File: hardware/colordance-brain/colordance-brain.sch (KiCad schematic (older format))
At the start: 21 parts, among them J1 Anderson, J5 RJ45, J6 RJ45, U1 AM26LS31x, U1 AP3211

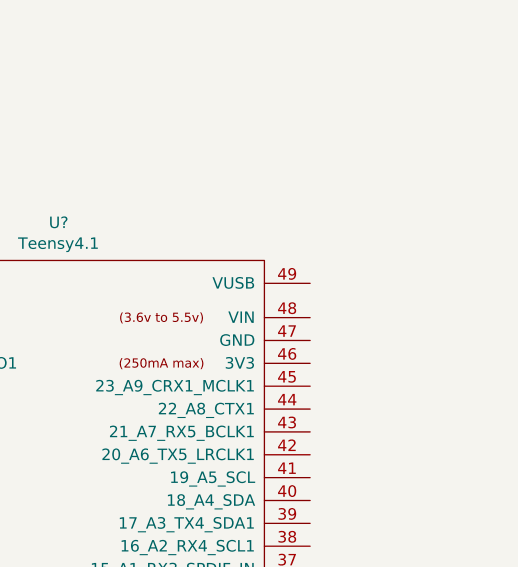
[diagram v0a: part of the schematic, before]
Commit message: Update pole node to v1.1
This adds lots of TVS diode, more decoupling, bulk caps on 5v and 12v
lines. Also adds pass-through Anderson connector.
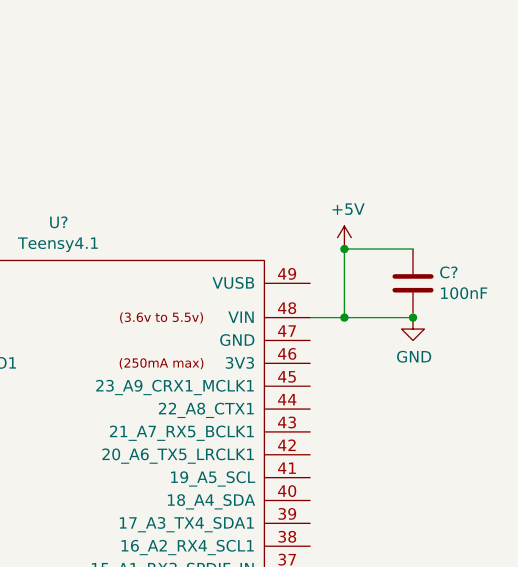
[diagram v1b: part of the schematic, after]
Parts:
- added C?: 100nF, symbol Device:C
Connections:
- net GND is gone; now on net +5V: C1.2, C1.2, C3.2, C?.2, C?.2, C?.2, C?.2, D1.2 (A), J1.2, J5.3, J5.4, J6.3, J6.4, R2.2, R5.2, U1.2 (GND), U1.8 (GND)
- net +5V: now also U?.48 (VIN), C?.1, C?.2
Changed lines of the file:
@@
 Wire Wire Line
 	1500 1250 1700 1250
+$Comp
+L power:+5V #PWR?
+U 1 1 60724EEF
+P 13100 2000
+F 0 "#PWR?" H 13100 1850 50  0001 C CNN
+F 1 "+5V" H 13115 2173 50  0000 C CNN
+F 2 "" H 13100 2000 50  0001 C CNN
+F 3 "" H 13100 2000 50  0001 C CNN
+	1    13100 2000
+	1    0    0    -1
+$EndComp
+Wire Wire Line
+	12950 2300 13100 2300
+Wire Wire Line
+	13100 2300 13100 2000
+$Comp
+L power:GND #PWR?
+U 1 1 60726663
+P 13400 2300
+F 0 "#PWR?" H 13400 2050 50  0001 C CNN
+F 1 "GND" H 13405 2127 50  0000 C CNN
+F 2 "" H 13400 2300 50  0001 C CNN
+F 3 "" H 13400 2300 50  0001 C CNN
+	1    13400 2300
+	1    0    0    -1
+$EndComp
+$Comp
+L Device:C C?
+U 1 1 60726AD1
+P 13400 2150
+F 0 "C?" H 13515 2196 50  0000 L CNN
+F 1 "100nF" H 13515 2105 50  0000 L CNN
+F 2 "" H 13438 2000 50  0001 C CNN
+F 3 "~" H 13400 2150 50  0001 C CNN
+	1    13400 2150
+	1    0    0    -1
+$EndComp
+Wire Wire Line
+	13100 2000 13400 2000
+Connection ~ 13100 2000
+Wire Wire Line
+	13400 2300 13100 2300
+Connection ~ 13400 2300
+Connection ~ 13100 2300
 $EndSCHEMATC

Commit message: More work on colordance-brain
- Define hierarchical sheet for RS422 output
- Update power supply
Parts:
- removed C1: .1uF, Capacitor_SMD:C_0603_1608Metric_Pad1.05x0.95mm_HandSolder, symbol Device:C
- removed C? (x4): 100nF, symbol Device:C
- removed J5, J6: RJ45, Connector_RJ:RJ45_Amphenol_54602-x08_Horizontal, symbol Connector:RJ45
- removed U1: AM26LS31x, Package_SO:SOIC-16_3.9x9.9mm_P1.27mm, symbol Homebrew:AM26LS31x
- added C10: .1uF, Capacitor_SMD:C_0603_1608Metric, symbol Device:C
- added C11, C12: 470uF, Capacitor_THT:CP_Radial_D10.0mm_P5.00mm, symbol Device:CP
- added D12: D_TVS_12V, Diode_SMD:D_SMB, symbol Device:D_TVS
- added D15: D_TVS_5V, Diode_SMD:D_SOD-523, symbol Device:D_TVS
- C2: MPN (none) -> CL10B122KB8NNNC
- D1: MPN (none) -> MBR230LSTR
- D2: MPN (none) -> 1N4148WS-7-F
- J1: footprint homebrew:Anderson_1337G3_right_angle_bottom_two -> homebrew:Anderson_1336G1_right_angle_bottom_two
- L1: MPN (none) -> NR6028T6R0M
- U1: MPN (none) -> AP3211KTR-G1
- gave numbers to parts that had none: 2
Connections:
- net +12V: now also C11.1, D12.1 (A1)
- net +5V: now also C10.1, C10.2, C11.2, C12.1, C12.2, D12.2 (A2), D15.1 (A1), D15.2 (A2)
- no-connect marks 1 -> 0
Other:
- moved on the sheet: C1, C2, C3, D1, D2, D4, J1, L1, R1, R2, R5, U1

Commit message: Colordance brain v1.0
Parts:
- added BT1: Battery_Cell, Battery:BatteryHolder_Keystone_3034_1x20mm, symbol Device:Battery_Cell
- added C11, C13, C15, C16, C17, C2, C3, C33, C6, C8, C9: 0.1uF, Capacitor_SMD:C_0603_1608Metric, symbol Device:C
- added D10, D12, D13, D15, D16, D17, D3, D4, D5, D6, D7, D8: D_TVS_5V, Diode_SMD:D_SMB, symbol Device:D_TVS
- added H1, H2, H3, H4: HOLE, homebrew:HOLE_5MM_#8, symbol Homebrew:HOLE
- added J2, J7: Conn_01x06, Connector_PinHeader_2.54mm:PinHeader_1x06_P2.54mm_Horizontal, symbol Connector_Generic:Conn_01x06
- added J3, J4, J5, J6: Conn_01x03, Connector_PinHeader_2.54mm:PinHeader_1x03_P2.54mm_Horizontal, symbol Connector_Generic:Conn_01x03
- added J8: Conn_01x05, Connector_PinHeader_2.54mm:PinHeader_1x05_P2.54mm_Horizontal, symbol Connector_Generic:Conn_01x05
- added R2: 1.2M, Resistor_SMD:R_0805_2012Metric, symbol Device:R
- added R3: 330k, Resistor_SMD:R_0603_1608Metric, symbol Device:R
- added U6, U7: 74AHCT1G126, Package_TO_SOT_SMD:SOT-353_SC-70-5, symbol 74xGxx:74AHCT1G126
- C10: renamed from C3; MPN (none) -> LMK212BBJ226MG-T
- C12: renamed from C10; value .1uF -> 0.1uF
- C4: value 100nF -> 0.1uF; footprint (none) -> Capacitor_SMD:C_0603_1608Metric
- D1: renamed from D4; MPN (none) -> 150060RS75000
- D14: renamed from D15; footprint Diode_SMD:D_SOD-523 -> Diode_SMD:D_SMB; MPN CPDH5V0U -> SMBJ6.0CD-M3/H
- R4: renamed from R1; MPN (none) -> RMCF0603FT11K5
- R5: renamed from R2; MPN (none) -> RC1608F2211CS
- U2: footprint (none) -> homebrew:Teensy41_stripped
- renumbered C11 to C1, C12 to C14, C1 to C5, C2 to C7, D2 to D11, D12 to D2, D1 to D9, R5 to R1
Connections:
- net +12V: now also R2.1
- net +5V: now also C13.1, C16.1, C2.1, C3.1, C8.1, C9.1, J2.6 (Pin_6), J3.3 (Pin_3), J4.3 (Pin_3), J5.3 (Pin_3), J6.3 (Pin_3), J7.6 (Pin_6), J8.5 (Pin_5), U6.1, U6.5 (VCC), U7.1, U7.5 (VCC); no longer C1.2, C10.2, C12.2, C14.2, C4.2, C5.2, D14.2 (A2), D2.2 (A2), D9.2 (A), J1.2, R1.2, R5.2, U1.2 (GND)
- net GND: now reaches U2.1 (GND)
- net GND: now also C1.2, C10.2, C12.2, C14.2, C4.2, C5.2, D14.2 (A2), D2.2 (A2), D9.2 (A), J1.2, R1.2, R5.2, U1.2 (GND), U2.47 (GND), BT1.2 (-), C11.2, C13.2, C15.2, C16.2, C17.2, C2.2, C3.2, C33.2, C6.2, C8.2, C9.2, D10.2 (A2), D12.2 (A2), D13.2 (A2), D15.2 (A2), D16.2 (A2), D17.2 (A2), D3.2 (A2), D4.2 (A2), D5.2 (A2), D6.2 (A2), D7.2 (A2), D8.2 (A2), J2.1 (Pin_1), J3.1 (Pin_1), J4.1 (Pin_1), J5.1 (Pin_1), J6.1 (Pin_1), J7.1 (Pin_1), J8.1 (Pin_1), R3.2, U6.3 (GND), U7.3 (GND)
- net CS_AUDIO: now reaches U2.11 (9_OUT1C)
- net CS_AUDIO: now also D17.1 (A1), J7.5 (Pin_5)
- net POLE4_PIR0: now reaches U2.12 (10_CS_MQSR)
- net POLE4_PIR1: now reaches U2.13 (11_MOSI_CTX1)
- net POLE3_PIR0: now reaches U2.14 (12_MISO_MQSL)
- net CONTROL_PANEL_LED: now reaches U2.16 (24_A10_TX6_SCL2)
- net CONTROL_PANEL_LED: now also U7.2
- net PODIUM_LED: now reaches U2.17 (25_A11_RX6_SDA2)
- net PODIUM_LED: now also U6.2
- net MOSI: now reaches U2.18 (26_A12_MOSI1)
- net MOSI: now also D16.1 (A1), D7.1 (A1), J2.4 (Pin_4), J7.4 (Pin_4)
- net SCK: now reaches U2.19 (27_A13_SCK1)
- net SCK: now also D13.1 (A1), D3.1 (A1), J2.2 (Pin_2), J7.2 (Pin_2)
- net POLE5_LED1: now reaches U2.2 (0_RX1_CRX2_CS1)
- net POLE3_PIR1: now reaches U2.20 (28_RX7)
- net POLE2_PIR1: now reaches U2.21 (29_TX7)
- net POLE0_PIR1: now reaches U2.25 (33_MCLK2)
- net POLE0_PIR0: now reaches U2.26 (34_RX8)
- net POLE1_PIR1: now reaches U2.27 (35_TX8)
- net POLE1_PIR0: now reaches U2.28 (36_CS)
- net POLE2_PIR0: now reaches U2.29 (37_CS)
- net POLE5_LED0: now reaches U2.3 (1_TX1_CTX2_MISO1)
- net CS_CTRL: now reaches U2.30 (38_CS1_IN1)
- net CS_CTRL: now also D8.1 (A1), J2.5 (Pin_5)
- net MISO: now reaches U2.31 (39_MISO1_OUT1A)
- net MISO: now also D15.1 (A1), D6.1 (A1), J2.3 (Pin_3), J7.3 (Pin_3)
- net AUX0: now reaches U2.32 (40_A16)
- net AUX0: now also J8.2 (Pin_2)
- net BATT_DIV: now reaches U2.33 (41_A17)
- net BATT_DIV: now also C33.1, R2.2, R3.1
- net POLE0_LED1: now reaches U2.36 (14_A0_TX3_SPDIF_OUT)
- net POLE0_LED0: now reaches U2.37 (15_A1_RX3_SPDIF_IN)
- net POLE1_LED0: now reaches U2.38 (16_A2_RX4_SCL1)
- net POLE1_LED1: now reaches U2.39 (17_A3_TX4_SDA1)
- net LOCAL_PIR1: now reaches U2.4 (2_OUT2)
- net LOCAL_PIR1: now also C11.1, D12.1 (A1), J6.2 (Pin_2)
- net POLE2_LED0: now reaches U2.40 (18_A4_SDA)
- net POLE2_LED1: now reaches U2.41 (19_A5_SCL)
- net POLE3_LED1: now reaches U2.42 (20_A6_TX5_LRCLK1)
- net POLE3_LED0: now reaches U2.43 (21_A7_RX5_BCLK1)
- net POLE4_LED0: now reaches U2.44 (22_A8_CTX1)
- net POLE4_LED1: now reaches U2.45 (23_A9_CRX1_MCLK1)
- net +3V3: now reaches U2.46 (3V3)
- net +3V3: now also C17.1, J8.4 (Pin_4)
- net LOCAL_PIR0: now reaches U2.5 (3_LRCLK2)
- net LOCAL_PIR0: now also C6.1, D5.1 (A1), J4.2 (Pin_2)
- net at U2.50 (VBAT): now also BT1.1 (+), C15.1
- net AUX1: now reaches U2.6 (4_BCLK2)
- net AUX1: now also J8.3 (Pin_3)
- net POLE5_PIR0: now reaches U2.7 (5_IN2)
- net POLE5_PIR1: now reaches U2.8 (6_OUT1D)
- new net: D4.1 (A1), J3.2 (Pin_2), U6.4
- new net: D10.1 (A1), J5.2 (Pin_2), U7.4
- no-connect marks 0 -> 26
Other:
- note added: "Local LEDs"
- note added: "Local PIR"
- note added: "Out To Poles"
- note added: "SPI to audio"
- note added: "SPI to control surface"
- moved on the sheet: D1, R1

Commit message: Random hardware changes
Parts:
- H1, H2, H3, H4: symbol Homebrew:HOLE -> colordance-brain-rescue:HOLE-Homebrew
- J1: symbol Homebrew:Anderson_two_redblack_src -> colordance-brain-rescue:Anderson_two_redblack_src-Homebrew
- U1: symbol Homebrew:AP3211 -> colordance-brain-rescue:AP3211-Homebrew
- U2: symbol teensy_library:Teensy4.1 -> colordance-brain-rescue:Teensy4.1-teensy_library
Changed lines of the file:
@@
 $EndComp
 $Comp
-L Homebrew:AP3211 U1
+L colordance-brain-rescue:AP3211-Homebrew U1
 U 1 1 5E594E3E
 P 2800 1400
@@
 	4400 1400 4700 1400
 $Comp
-L Homebrew:Anderson_two_redblack_src J1
+L colordance-brain-rescue:Anderson_two_redblack_src-Homebrew J1
 U 1 1 5E5A16EF
 P 700 1300
@@
 $EndComp
 $Comp
-L Homebrew:HOLE H1
+L colordance-brain-rescue:HOLE-Homebrew H1
 U 1 1 60A08675
 P 10450 8500
@@
 $EndComp
 $Comp
-L Homebrew:HOLE H2
+L colordance-brain-rescue:HOLE-Homebrew H2
 U 1 1 60A09861
 P 10450 8750
@@
 $EndComp
 $Comp
-L Homebrew:HOLE H3
+L colordance-brain-rescue:HOLE-Homebrew H3
 U 1 1 60A09A47
 P 10450 9000
@@
 $EndComp
 $Comp
-L Homebrew:HOLE H4
+L colordance-brain-rescue:HOLE-Homebrew H4
 U 1 1 60A09CE3
 P 10450 9250
@@
 CS_AUDIO
 $Comp
-L teensy_library:Teensy4.1 U2
+L colordance-brain-rescue:Teensy4.1-teensy_library U2
 U 1 1 607BEEC0
 P 11850 4450
